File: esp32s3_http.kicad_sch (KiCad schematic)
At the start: 40 parts, among them J1 USB_B, J2 Jack-DC, J3 EXP1_UART, J4 EXP2, SW1 SW_Push, SW2 SW_Push, U1 ESP32-S3-WROOM-1, U2 LM2940T-3.3, U3 NJM7805FA, Y1 32.768KHz

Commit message: SW1/SW2 と J2 を秋月品 (TS-06104 / MJ-179PH) 用フットプリントに変更
- プロジェクトローカルライブラリ esp32s3_http.pretty を追加 (${KIPRJMOD})
- SW_TS-06104: データシート P.C.B LAYOUT 準拠 (10.0/6.4 x 5.5/3.5)
- DCJack_MJ-179PH: スロット穴 3 本、部品面視 (データシートの穴図は半田面視)

Co-Authored-By: Claude Opus 5.5 <noreply@anthropic.com>
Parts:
- J2: value Jack-DC -> MJ-179PH; footprint Connector_BarrelJack:BarrelJack_GCT_DCJ200-10-A_Horizontal -> esp32s3_http:DCJack_MJ-179PH
- SW1, SW2: value SW_Push -> TS-06104; footprint Button_Switch_SMD:SW_Push_1P1T_NO_CK_KSC6xxJ -> esp32s3_http:SW_TS-06104
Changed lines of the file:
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@@
 			)
 		)
-		(property "Value" "SW_Push"
+		(property "Value" "TS-06104"
 			(at 87.63 129.54 0)
 			(show_name no)
@@
 			)
 		)
-		(property "Footprint" "Button_Switch_SMD:SW_Push_1P1T_NO_CK_KSC6xxJ"
+		(property "Footprint" "esp32s3_http:SW_TS-06104"
 			(at 87.63 129.54 0)
 			(hide yes)
@@
 			)
 		)
-		(property "Value" "SW_Push"
+		(property "Value" "TS-06104"
 			(at 120.65 130.81 0)
 			(show_name no)
@@
 			)
 		)
-		(property "Footprint" "Button_Switch_SMD:SW_Push_1P1T_NO_CK_KSC6xxJ"
+		(property "Footprint" "esp32s3_http:SW_TS-06104"
 			(at 120.65 130.81 0)
 			(hide yes)
@@
 			)
 		)
-		(property "Value" "Jack-DC"
+		(property "Value" "MJ-179PH"
 			(at 153.67 22.86 0)
 			(show_name no)
@@
 			)
 		)
-		(property "Footprint" "Connector_BarrelJack:BarrelJack_GCT_DCJ200-10-A_Horizontal"
+		(property "Footprint" "esp32s3_http:DCJack_MJ-179PH"
 			(at 154.94 30.226 0)
 			(hide yes)

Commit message: J1 を秋月品 USB-B (5075BR-04) 用フットプリントに変更
- データシート PCB LAYOUT 準拠: 信号 2.50x2.00 d0.92, シェル 12.04 間隔 d2.30
- 旧 Lumberg 2411-02 からシェル穴位置が 0.15mm 異なる

Co-Authored-By: Claude Opus 5.5 <noreply@anthropic.com>
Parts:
- J1: value USB_B -> 5075BR-04; footprint Connector_USB:USB_B_Lumberg_2411_02_Horizontal -> esp32s3_http:USB_B_5075BR-04
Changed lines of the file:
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@@
 			)
 		)
-		(property "Value" "USB_B"
+		(property "Value" "5075BR-04"
 			(at 40.64 35.56 0)
 			(show_name no)
@@
 			)
 		)
-		(property "Footprint" "Connector_USB:USB_B_Lumberg_2411_02_Horizontal"
+		(property "Footprint" "esp32s3_http:USB_B_5075BR-04"
 			(at 44.45 46.99 0)
 			(hide yes)

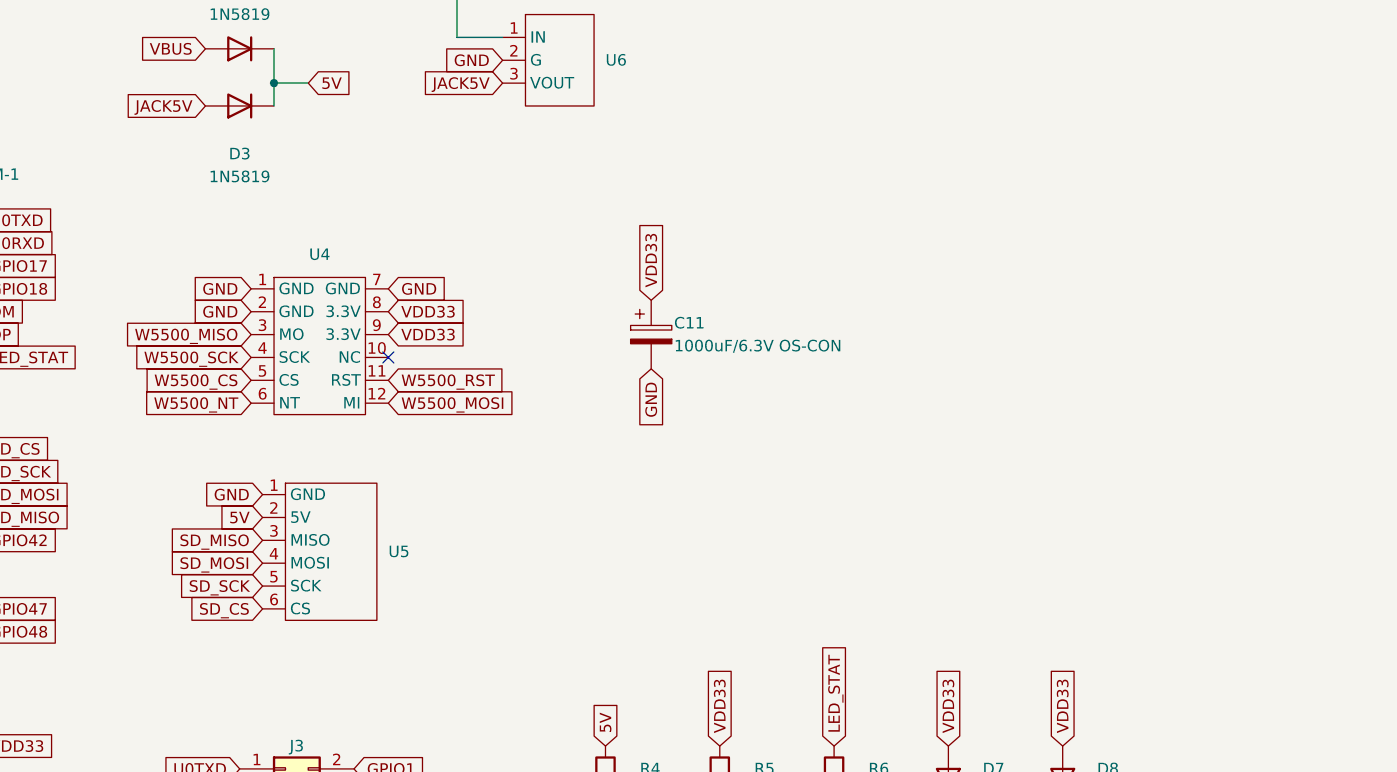
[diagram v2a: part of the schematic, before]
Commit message: W5500/SD の電源電圧をはんだジャンパで切替可能に (JP1/JP2)
3 パッドのはんだジャンパ (1-2 パターン接続済み) を B 面に追加。
既定値は従来どおりで、変更時は 1-2 間をカットし 2-3 をはんだでブリッジする。

- JP1 (W5500, U4 の裏): 1=VDD33 (既定) / 2=W5500_VCC / 3=5V
- JP2 (SD, U5 ピン列の左): 1=5V (既定) / 2=SD_VCC / 3=VDD33
- C11 (W5500 給電点の OS-CON) は W5500_VCC 側に移動 (6.3V 品なので 5V でも可)
- B 面シルクに切替方法を表記、回路図に注記を追加
- ERC 0、DRC は既存の警告のみ (未接続 0、回路図との差異 0)

Co-Authored-By: Claude Opus 5.5 <noreply@anthropic.com>
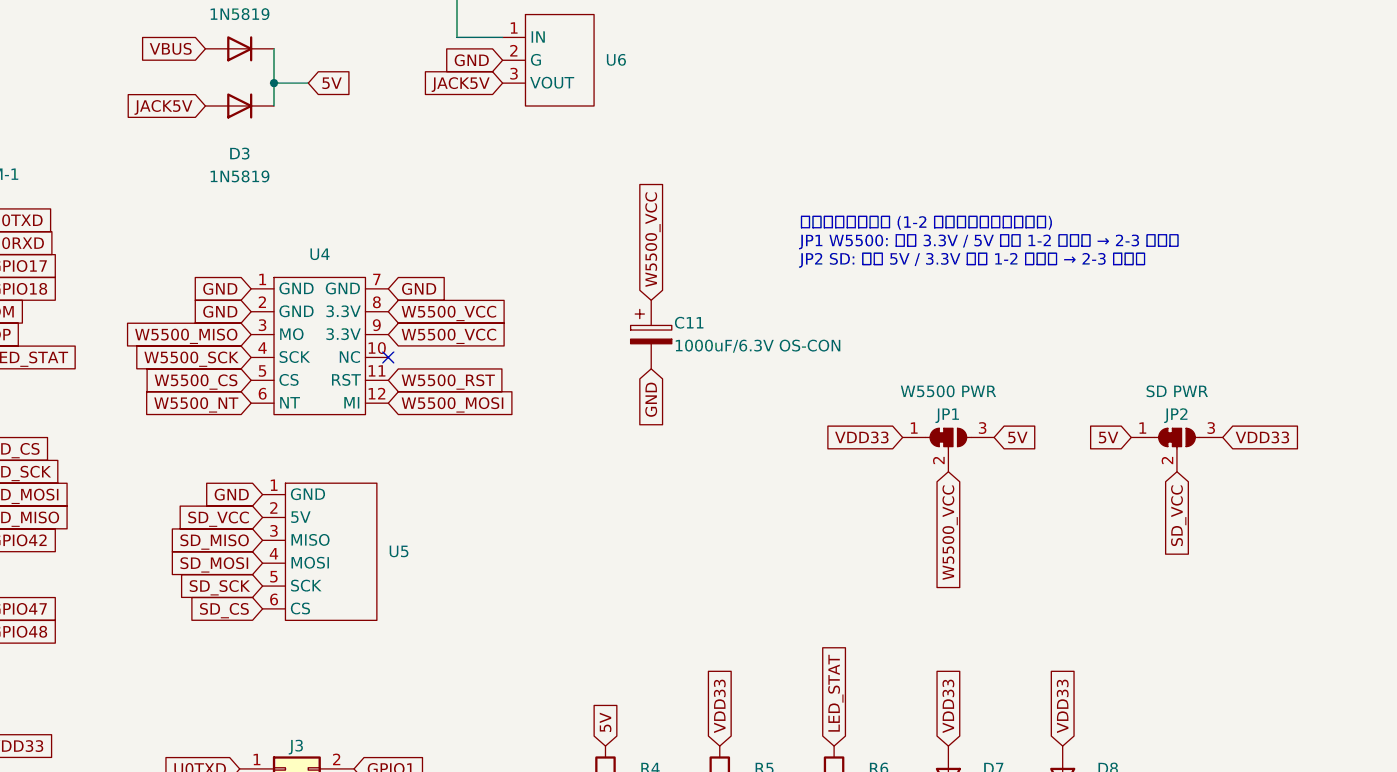
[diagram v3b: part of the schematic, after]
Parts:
- added JP1: W5500 PWR, Jumper:SolderJumper-3_P1.3mm_Bridged12_RoundedPad1.0x1.5mm_NumberLabels, symbol Jumper:SolderJumper_3_Bridged12
- added JP2: SD PWR, Jumper:SolderJumper-3_P1.3mm_Bridged12_RoundedPad1.0x1.5mm_NumberLabels, symbol Jumper:SolderJumper_3_Bridged12
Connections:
- net 5V: now also JP1.3 (B), JP2.1 (A); no longer U5.2 (5V)
- net VDD33: now also JP1.1 (A), JP2.3 (B); no longer C11.1, U4.8 (3.3V), U4.9 (3.3V)
- new net SD_VCC: JP2.2 (C), U5.2 (5V)
- new net W5500_VCC: C11.1, JP1.2 (C), U4.8 (3.3V), U4.9 (3.3V)
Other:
- note added: "電源切替ジャンパ (1-2 はパターンで接続済み) JP1 W5500: 既定 3.3V / 5V 化は 1-2 カット → 2-3 ハンダ JP2 SD: 既定 5V / 3.3V 化は 1-2 カット → 2-3 ハンダ"
